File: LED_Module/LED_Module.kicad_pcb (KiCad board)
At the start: 2 copper layers, 19 parts, among them J1 Conn_02x05_Odd_Even, J2 Conn_01x03_Male, SW1 SW_Push, U1 LD1117S33TR_SOT223, U2 STM32F091RCTx

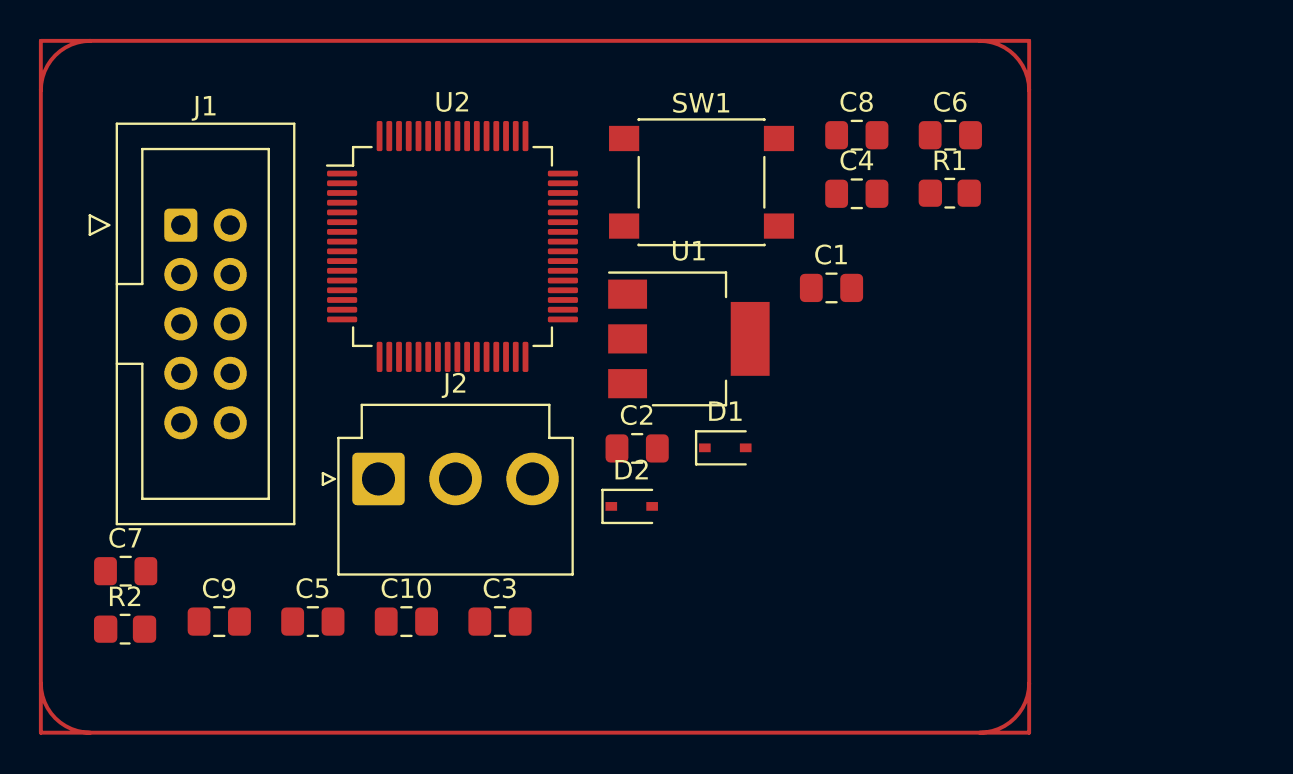
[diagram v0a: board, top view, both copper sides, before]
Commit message: Buck Converter and Wifi schematic
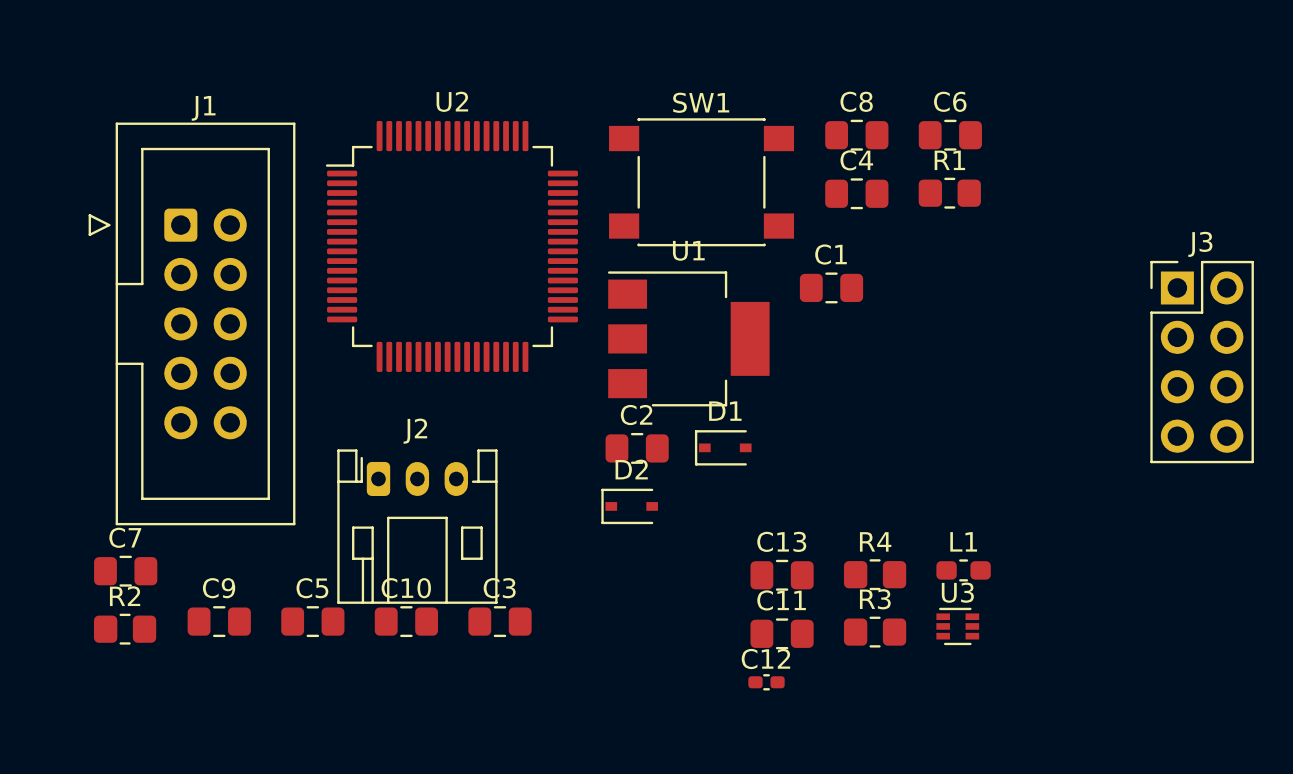
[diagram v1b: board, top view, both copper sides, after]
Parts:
- added C11: CIN, Capacitor_SMD:C_0805_2012Metric_Pad1.18x1.45mm_HandSolder, F.Cu at (139.7, 116.8)
- added C12: Cff, Capacitor_SMD:C_0402_1005Metric_Pad0.74x0.62mm_HandSolder, F.Cu at (138.9, 119.3)
- added C13: Cout, Capacitor_SMD:C_0805_2012Metric_Pad1.18x1.45mm_HandSolder, F.Cu at (139.7, 113.8)
- added J3: Conn_02x04_Counter_Clockwise, Connector_PinHeader_2.54mm:PinHeader_2x04_P2.54mm_Vertical, F.Cu at (160.0, 99.1)
- added L1: L1, Inductor_SMD:L_0603_1608Metric_Pad1.05x0.95mm_HandSolder, F.Cu at (149.0, 113.6)
- added R3: Rfbt, Resistor_SMD:R_0805_2012Metric_Pad1.20x1.40mm_HandSolder, F.Cu at (144.5, 116.8)
- added R4: rFBB, Resistor_SMD:R_0805_2012Metric_Pad1.20x1.40mm_HandSolder, F.Cu at (144.5, 113.8)
- added U3: TPS62A02DRL, Package_TO_SOT_SMD:SOT-563, F.Cu at (148.7, 116.5)
- J2: footprint Connector_JST:JST_VH_B3P-VH-B_1x03_P3.96mm_Vertical -> Connector_JST:JST_PH_S3B-PH-K_1x03_P2.00mm_Horizontal

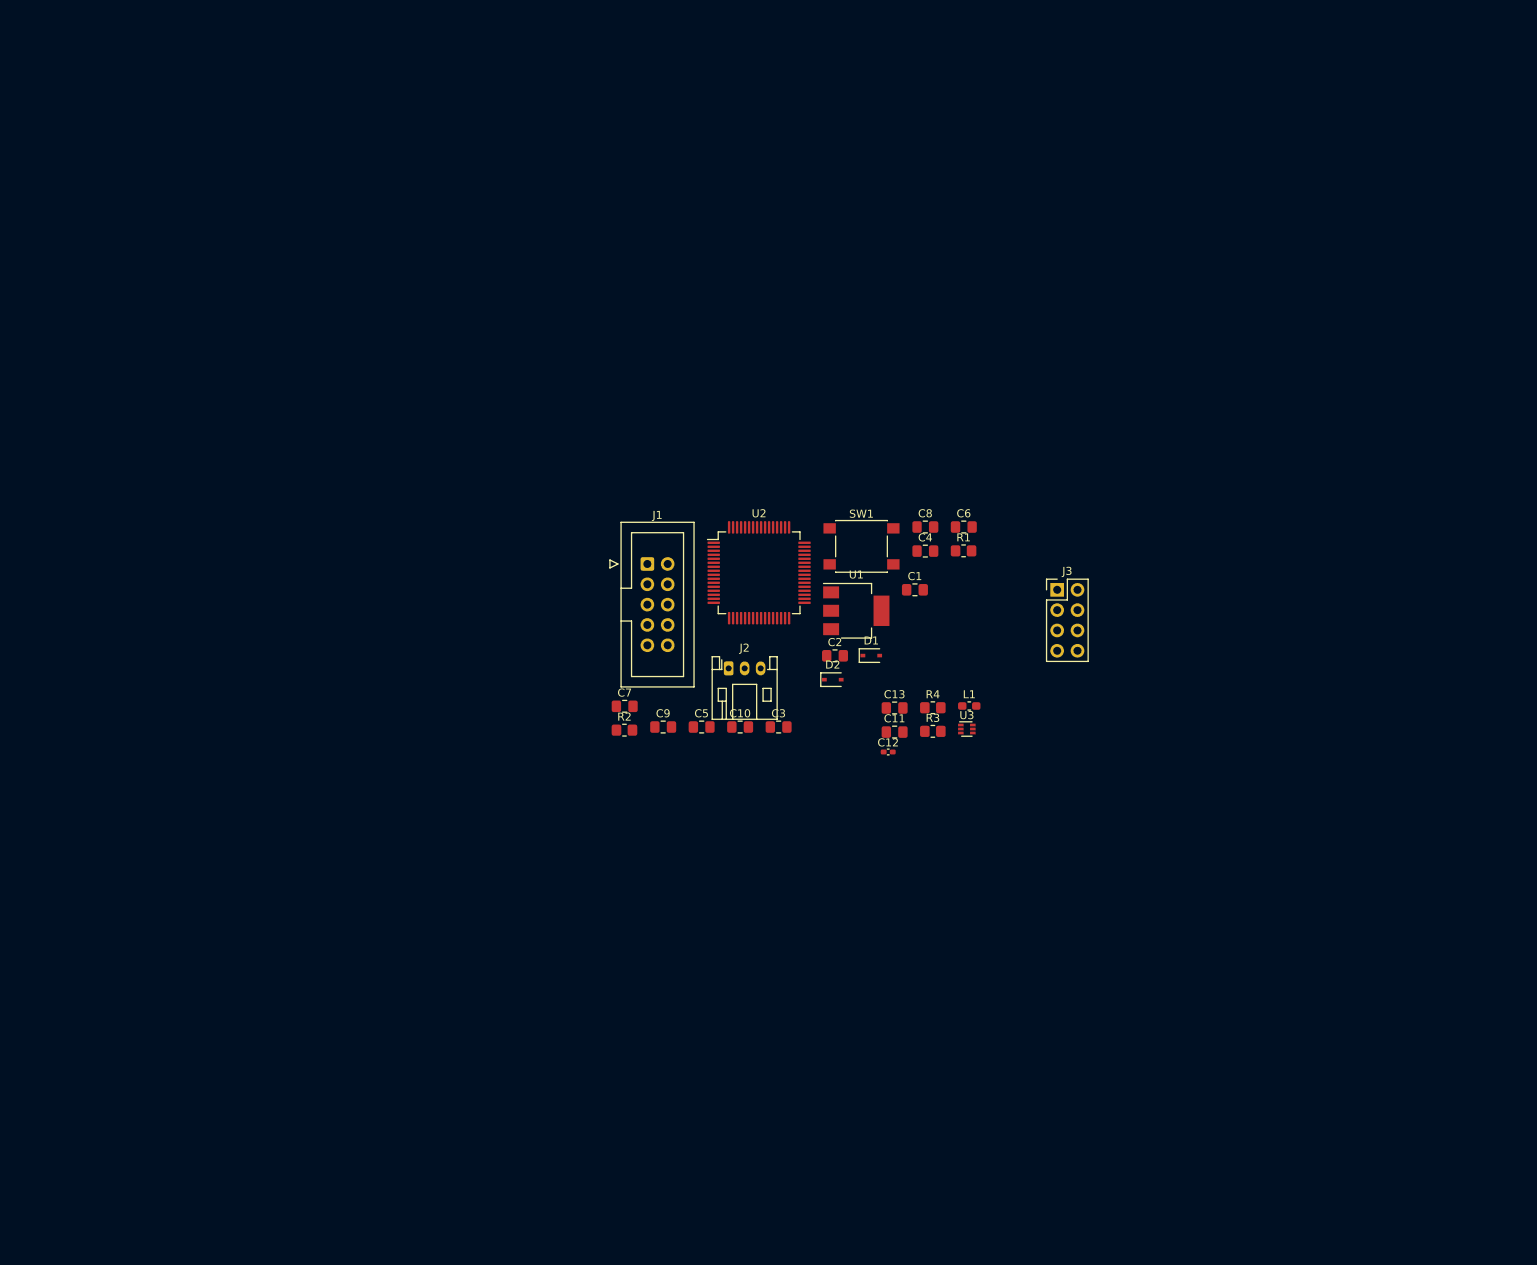
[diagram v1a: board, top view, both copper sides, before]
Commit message: EEPROM Schematic, Decoupling routing, Buck Layout
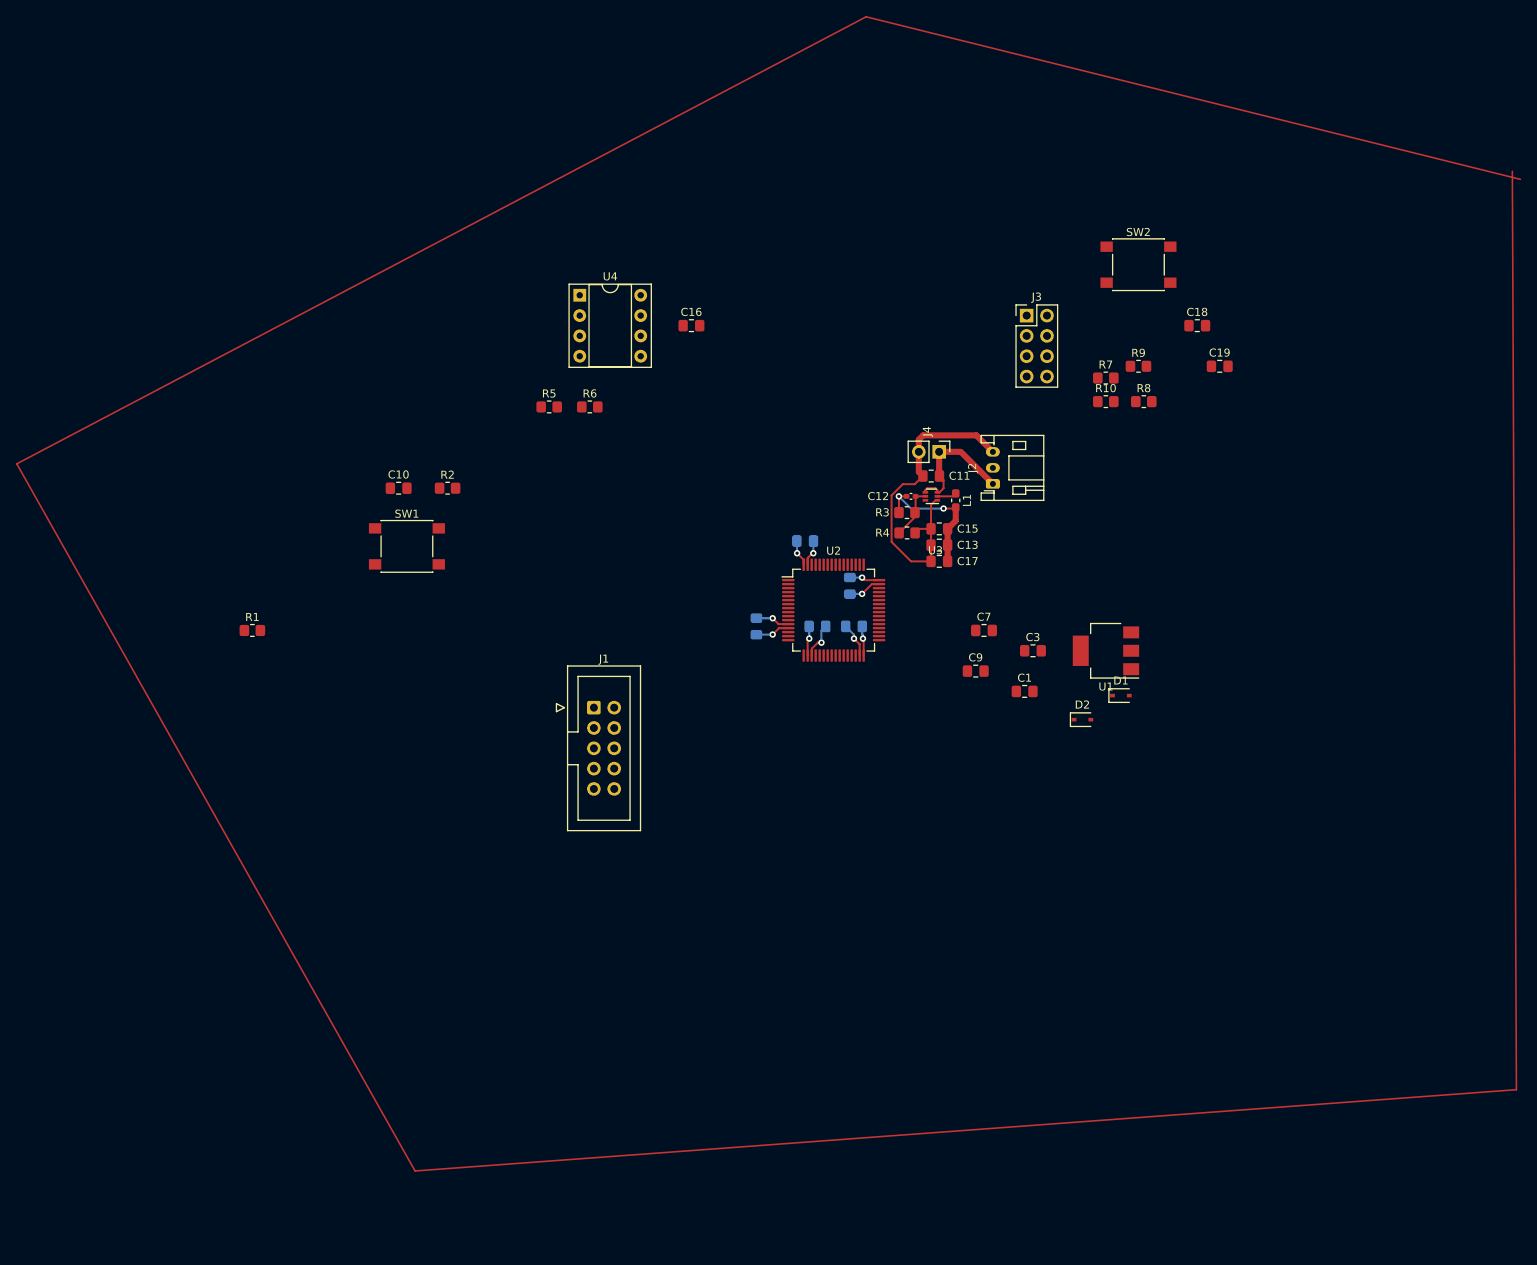
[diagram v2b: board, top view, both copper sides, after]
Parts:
- added C15: Cout, Capacitor_SMD:C_0805_2012Metric_Pad1.18x1.45mm_HandSolder, F.Cu at (145.3, 91.4)
- added C16: 0.1 uF, Capacitor_SMD:C_0805_2012Metric_Pad1.18x1.45mm_HandSolder, F.Cu at (114.3, 66.0)
- added C17: Cout, Capacitor_SMD:C_0805_2012Metric_Pad1.18x1.45mm_HandSolder, F.Cu at (145.3, 95.5)
- added C18: 0.1 uF, Capacitor_SMD:C_0805_2012Metric_Pad1.18x1.45mm_HandSolder, F.Cu at (177.5, 66.0)
- added C19: 500 nF, Capacitor_SMD:C_0805_2012Metric_Pad1.18x1.45mm_HandSolder, F.Cu at (180.3, 71.1)
- added J4: Barrel_Jack, Connector_PinHeader_2.54mm:PinHeader_1x02_P2.54mm_Vertical, F.Cu at (145.3, 81.8)
- added R10: R, Resistor_SMD:R_0805_2012Metric_Pad1.20x1.40mm_HandSolder, F.Cu at (166.1, 75.5)
- added R5: 2K, Resistor_SMD:R_0805_2012Metric_Pad1.20x1.40mm_HandSolder, F.Cu at (96.5, 76.2)
- added R6: 2K, Resistor_SMD:R_0805_2012Metric_Pad1.20x1.40mm_HandSolder, F.Cu at (101.6, 76.2)
- added R7: R, Resistor_SMD:R_0805_2012Metric_Pad1.20x1.40mm_HandSolder, F.Cu at (166.1, 72.6)
- added R8: 100K, Resistor_SMD:R_0805_2012Metric_Pad1.20x1.40mm_HandSolder, F.Cu at (170.8, 75.5)
- added R9: R, Resistor_SMD:R_0805_2012Metric_Pad1.20x1.40mm_HandSolder, F.Cu at (170.2, 71.1)
- added SW2: SW_Push, Button_Switch_SMD:SW_SPST_PTS645, F.Cu at (170.2, 58.4)
- added U4: 24AA32AF EEPROM, Package_DIP:DIP-8_W7.62mm_Socket, F.Cu at (100.3, 62.2)
- C2, C4, C5, C6, C8: moved to B.Cu
- J3: value Conn_02x04_Counter_Clockwise -> ESP8266 Header
- moved R1 89.5 mm to (59.4, 104.1)
- moved SW1 56.8 mm to (78.7, 93.6)
- moved C10 52.1 mm to (77.7, 86.4)
- moved C7 45.9 mm to (150.9, 104.1)
- moved J2 40.3 mm to (152.0, 85.8), turned to 90 degrees
- moved C9 39.7 mm to (149.8, 109.2)
- moved R2 37.5 mm to (83.8, 86.4)
- moved J3 34.5 mm to (156.2, 64.8)
- moved C3 33.2 mm to (157.0, 106.7)
- moved C11 32.3 mm to (144.3, 84.8), turned to 180 degrees
- moved C12 32.1 mm to (141.8, 87.4)
- moved U1 31.6 mm to (166.1, 106.7), turned to 180 degrees
- moved D1 31.6 mm to (168.0, 112.3)
- moved D2 31.6 mm to (163.2, 115.3)
- moved U3 29.4 mm to (144.3, 87.4), turned to 180 degrees
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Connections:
- C12 pad 1: Net-(C12-Pad1) -> 3.3V
- C13 pad 1: Net-(C12-Pad1) -> 3.3V
- J3 pad 1: unconnected-(J3-Pad1) -> /PD2
- J3 pad 2: unconnected-(J3-Pad2) -> /CH_PD
- J3 pad 3: unconnected-(J3-Pad3) -> /RST
- J3 pad 4: unconnected-(J3-Pad4) -> 3.3V
- J3 pad 5: unconnected-(J3-Pad5) -> /PC12
- J3 pad 6: unconnected-(J3-Pad6) -> /GPIO0
- J3 pad 7: unconnected-(J3-Pad7) -> /GPIO2
- J3 pad 8: unconnected-(J3-Pad8) -> GND
- L1 pad 2: Net-(C12-Pad1) -> 3.3V
- R3 pad 1: Net-(C12-Pad1) -> 3.3V
- U2 pad 58: /PB6 -> /EEPROM_SCL
- U2 pad 59: /PB7 -> /EEPROM_SDA
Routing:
- net GND: track 0.00 -> 61.7 mm, vias 0 -> 5
- net 3.3V: track 0.00 -> 37.7 mm, vias 0 -> 7
- net 5V: track 0.00 -> 16.4 mm
- net Net-(C12-Pad2): track 0.00 -> 6.71 mm
- net Net-(L1-Pad1): track 0.00 -> 2.45 mm

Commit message: Revision to Buck Layout
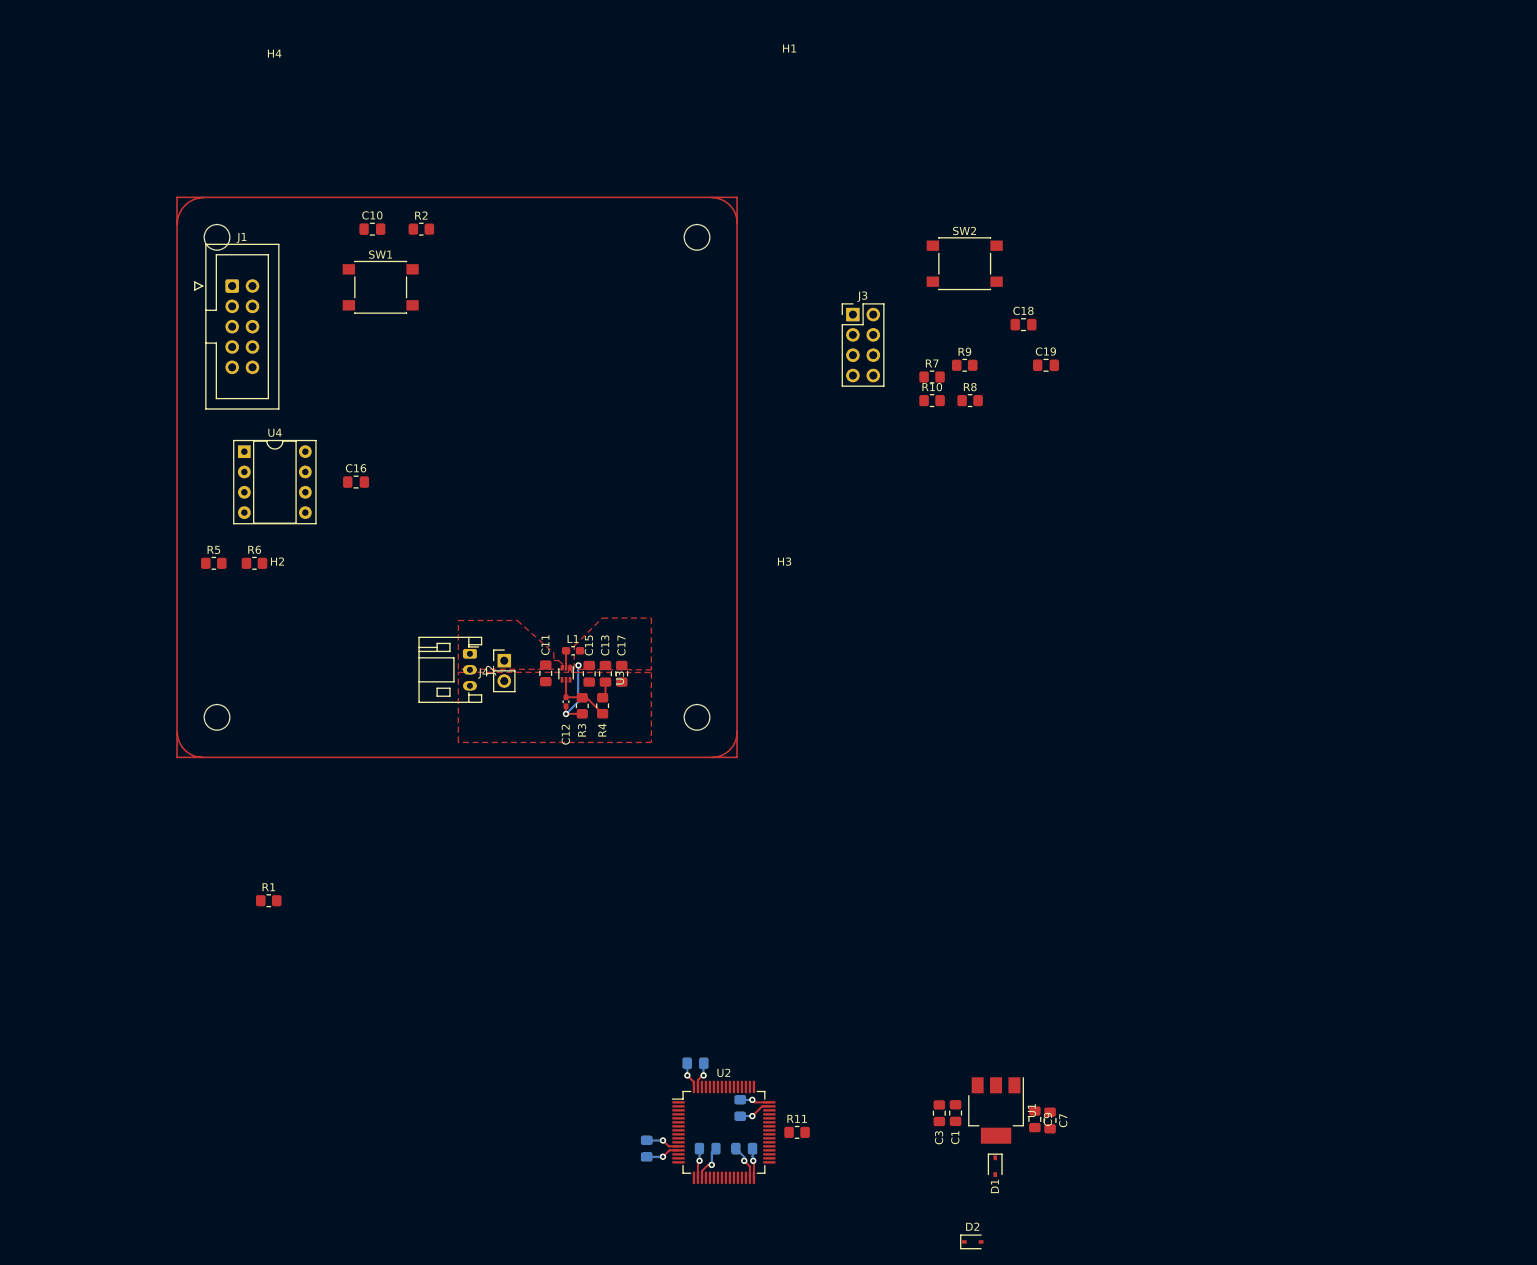
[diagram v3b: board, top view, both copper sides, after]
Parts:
- added H1: MountingHole, MountingHole:MountingHole_3.2mm_M3, F.Cu at (126.6, 35.6)
- added H2: MountingHole, MountingHole:MountingHole_3.2mm_M3, F.Cu at (62.6, 99.8)
- added H3: MountingHole, MountingHole:MountingHole_3.2mm_M3, F.Cu at (125.9, 99.8)
- added H4: MountingHole, MountingHole:MountingHole_3.2mm_M3, F.Cu at (62.2, 36.3)
- added R11: R, Resistor_SMD:R_0805_2012Metric_Pad1.20x1.40mm_HandSolder, F.Cu at (127.5, 166.9)
- moved J1 69.4 mm to (56.9, 61.1)
- moved J2 68.7 mm to (86.6, 107.1), turned to -90 degrees
- moved C2 66.7 mm to (116.3, 168.9)
- moved C5 66.7 mm to (120.9, 168.9)
- moved C6 66.7 mm to (120.4, 163.8)
- moved D2 66.7 mm to (149.5, 180.6)
- moved U2 66.7 mm to (118.4, 166.9)
- moved C4 66.7 mm to (114.8, 158.2)
- moved C8 66.7 mm to (108.7, 168.9)
- moved C7 61.8 mm to (159.1, 165.4), turned to -90 degrees
- moved D1 60.9 mm to (152.3, 171.1), turned to -90 degrees
- moved J4 60.3 mm to (90.9, 107.9), turned to 0 degrees
- moved U1 59.1 mm to (152.4, 164.1), turned to -90 degrees
- moved C3 59.0 mm to (145.3, 164.5), turned to -90 degrees
- moved C9 56.5 mm to (157.2, 165.2), turned to -90 degrees
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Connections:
- C11 pad 2: GND -> BUCK_GND
- C13 pad 2: GND -> BUCK_GND
- C15 pad 2: GND -> BUCK_GND
- C17 pad 2: GND -> BUCK_GND
- J2 pad 2: PA8 -> Net-(J2-Pad2)
- J2 pad 3: GND -> BUCK_GND
- J4 pad 2: GND -> BUCK_GND
- R4 pad 2: GND -> BUCK_GND
- U3 pad 1: GND -> BUCK_GND
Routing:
- net GND: track 61.7 -> 19.9 mm
- net 5V: track 16.4 -> 0.06 mm
- net 3.3V: track 37.7 -> 29.5 mm
- net BUCK_GND: track 0.00 -> 2.10 mm
- net Net-(C12-Pad2): track 6.71 -> 7.66 mm
- net Net-(L1-Pad1): track 2.45 -> 1.93 mm
- added copper zone on F.Cu, net 3.3V
- added copper zone on F.Cu, net 5V
- added copper zone on F.Cu, net BUCK_GND
